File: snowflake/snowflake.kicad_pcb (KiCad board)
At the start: 2 copper layers, 150.2 x 150.2 mm, 72 parts, among them J3 TC2030, SW1 SK-12E12-G040, U1 TZ-5050S2RGB-5V-I4-H1, U10 TZ-5050S2RGB-5V-I4-H1, U11 TZ-5050S2RGB-5V-I4-H1, U12 TZ-5050S2RGB-5V-I4-H1, U13 TZ-5050S2RGB-5V-I4-H1, U14 TZ-5050S2RGB-5V-I4-H1, U15 TZ-5050S2RGB-5V-I4-H1, U16 TZ-5050S2RGB-5V-I4-H1, U17 TZ-5050S2RGB-5V-I4-H1, U18 TZ-5050S2RGB-5V-I4-H1, U19 TZ-5050S2RGB-5V-I4-H1, U2 TZ-5050S2RGB-5V-I4-H1, U20 TZ-5050S2RGB-5V-I4-H1, U21 TZ-5050S2RGB-5V-I4-H1, U22 TZ-5050S2RGB-5V-I4-H1, U23 TZ-5050S2RGB-5V-I4-H1, U24 TZ-5050S2RGB-5V-I4-H1, U25 TPS61022, U26 CH32V003F4U6, U3 TZ-5050S2RGB-5V-I4-H1, U4 TZ-5050S2RGB-5V-I4-H1, U5 TZ-5050S2RGB-5V-I4-H1, U6 TZ-5050S2RGB-5V-I4-H1, U7 TZ-5050S2RGB-5V-I4-H1, U8 TZ-5050S2RGB-5V-I4-H1, U9 TZ-5050S2RGB-5V-I4-H1

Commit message: Add mounting and tooling holes
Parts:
- added REF**: ToolingHole_1.152mm, MountingHole:ToolingHole_1.152mm, F.Cu at (150.0, 218.0)
- added REF**: ToolingHole_1.152mm, MountingHole:ToolingHole_1.152mm, F.Cu at (110.0, 150.0)
- added REF**1: ToolingHole_1.152mm, MountingHole:ToolingHole_1.152mm, F.Cu at (130.0, 184.6)
- added REF**10: ToolingHole_1.152mm, MountingHole:ToolingHole_1.152mm, F.Cu at (130.0, 115.4)
- added REF**2: ToolingHole_1.152mm, MountingHole:ToolingHole_1.152mm, F.Cu at (208.9, 184.0)
- added REF**3: ToolingHole_1.152mm, MountingHole:ToolingHole_1.152mm, F.Cu at (170.0, 184.6)
- added REF**4: ToolingHole_1.152mm, MountingHole:ToolingHole_1.152mm, F.Cu at (208.9, 116.0)
- added REF**5: ToolingHole_1.152mm, MountingHole:ToolingHole_1.152mm, F.Cu at (190.0, 150.0)
- added REF**6: MountingHole_2.1mm, MountingHole:MountingHole_2.1mm, F.Cu at (150.0, 82.0)
- added REF**7: ToolingHole_1.152mm, MountingHole:ToolingHole_1.152mm, F.Cu at (91.1, 116.0)
- added REF**8: ToolingHole_1.152mm, MountingHole:ToolingHole_1.152mm, F.Cu at (170.0, 115.4)
- added REF**9: ToolingHole_1.152mm, MountingHole:ToolingHole_1.152mm, F.Cu at (91.1, 184.0)

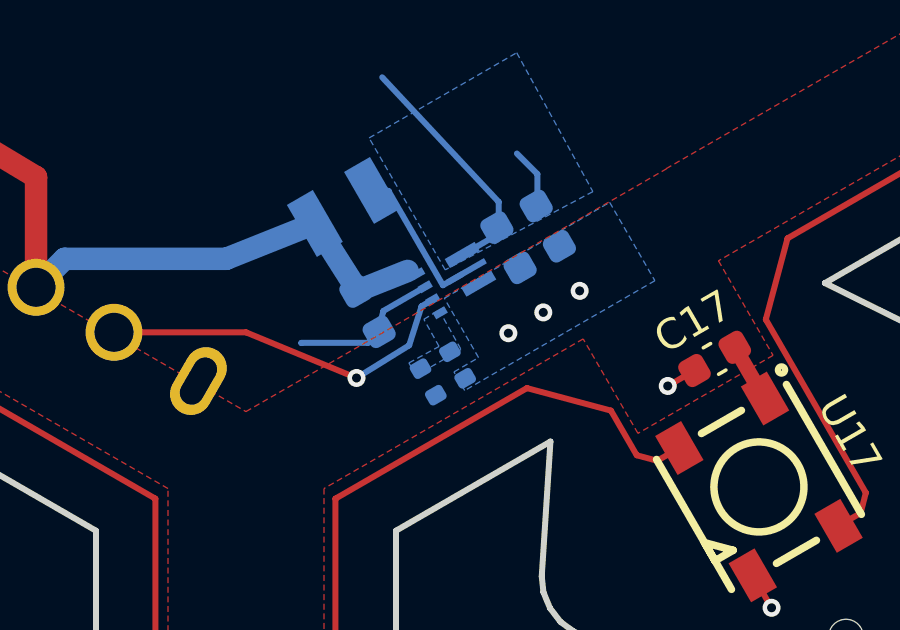
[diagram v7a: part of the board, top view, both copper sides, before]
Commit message: Use basic parts, fix boost converter positioning
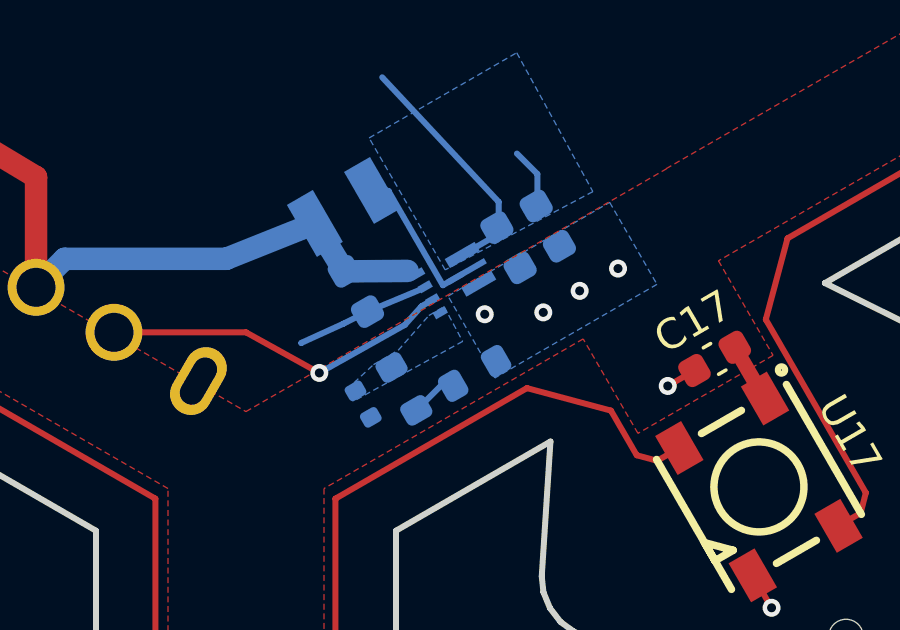
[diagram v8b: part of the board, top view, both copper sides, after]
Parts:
- added R0: 510k, Resistor_SMD:R_0603_1608Metric, B.Cu at (157.6, 175.9)
- R1: value 732k -> 220k; footprint Resistor_SMD:R_0402_1005Metric -> Resistor_SMD:R_0603_1608Metric
- R5, R6, R7: value 560k -> 510k
- moved R2 2.29 mm to (153.9, 176.9)
- moved R1 1.96 mm to (155.3, 176.4)
- moved C27 0.78 mm to (153.7, 173.1)
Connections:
- R1 pad 1: +5V -> Net-(R0-Pad1)
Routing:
- net Net-(R0-Pad1): track 0.00 -> 1.57 mm
- net /EN: track 12.1 -> 11.5 mm
- net +5V: vias 5 -> 6
